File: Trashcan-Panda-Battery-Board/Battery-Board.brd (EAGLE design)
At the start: 77.5 x 45.4 mm, 5 parts, among them J1 B2B-PH-SM4-TB(LF)(SN)

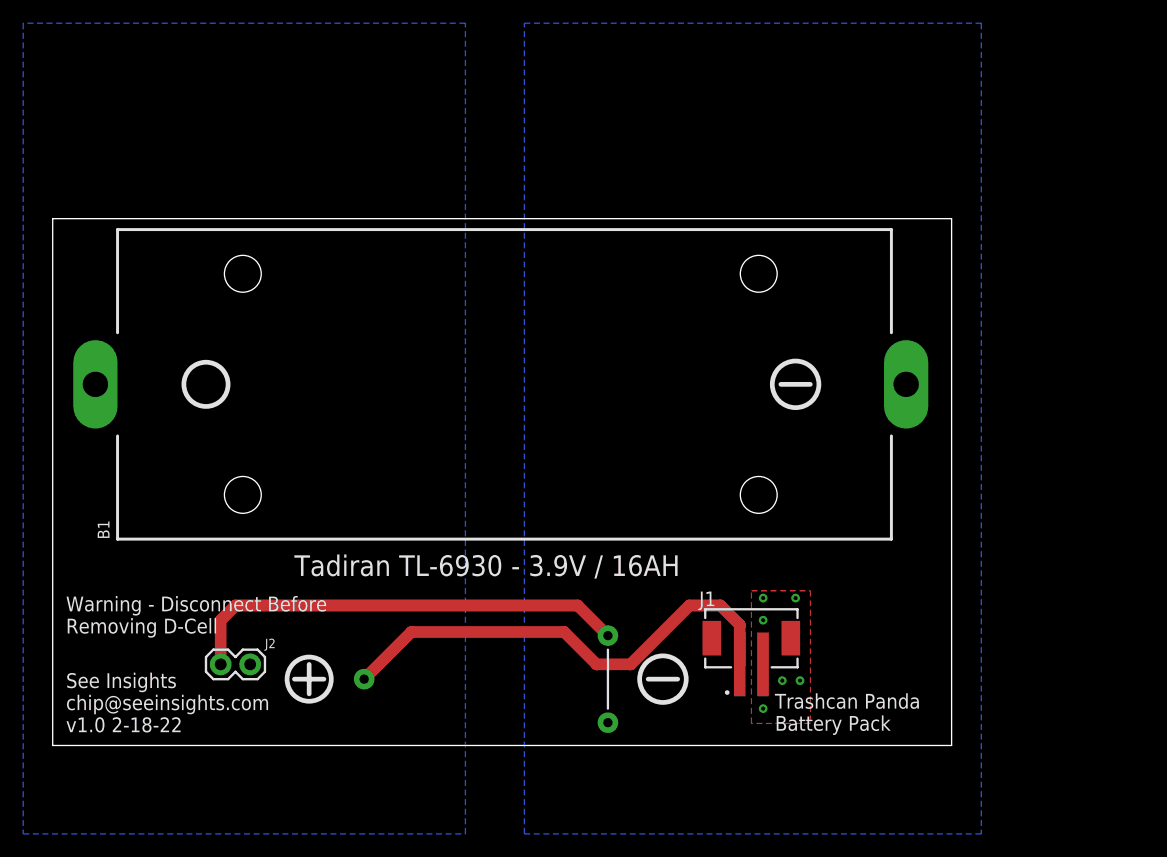
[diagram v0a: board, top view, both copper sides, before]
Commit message: Updated battery board to v1.1
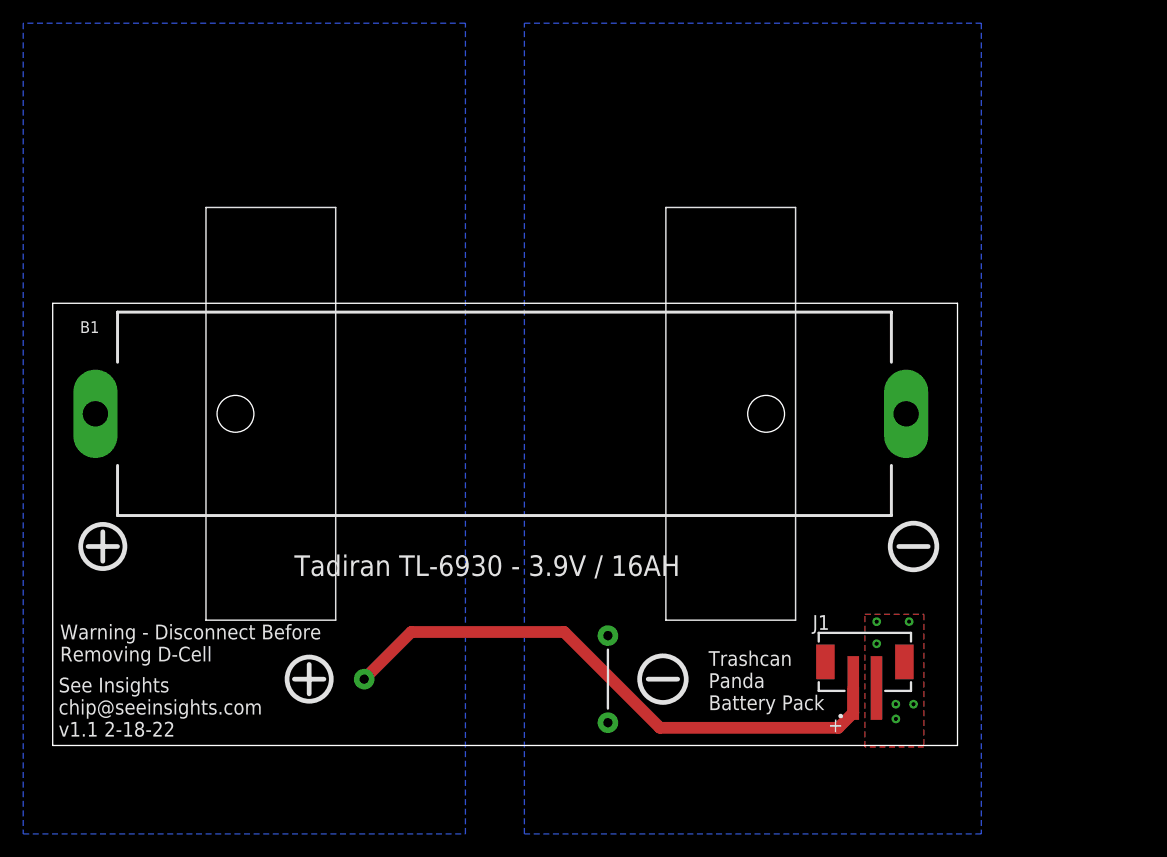
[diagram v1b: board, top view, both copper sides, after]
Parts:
- removed J2: (no value), SparkFun-Connectors:1X02
- B1: value 2226 -> 2232; device Battery-Board:2226 -> Battery-Board:2232
- moved J1 9.99 mm to (70.0, 4.95)
- moved B1 2.54 mm to (38.6, 28.6)
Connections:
- net GND: no longer J2.1
- net VCC: no longer J2.2
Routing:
- net GND: track 38.8 -> 0.00 mm
- net VCC: track 41.4 -> 49.9 mm
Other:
- board size 77.5 x 45.4 mm -> 78 x 38.1 mm
- board text added: "+"
- board text added: "See Insights chip@seeinsights.com v1.1 2-18-22"
- board text removed: "See Insights chip@seeinsights.com v1.0 2-18-22"
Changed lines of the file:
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@@
 <board>
 <plain>
-<wire x1="0" y1="0" x2="77.45" y2="0" width="0" layer="20"/>
-<wire x1="77.45" y1="0" x2="77.45" y2="45.39" width="0" layer="20"/>
-<wire x1="77.45" y1="45.39" x2="0" y2="45.39" width="0" layer="20"/>
-<wire x1="0" y1="45.39" x2="0" y2="0" width="0" layer="20"/>
-<text x="62.23" y="1.27" size="1.27" layer="21">Trashcan Panda
+<wire x1="0" y1="0" x2="77.958" y2="0" width="0" layer="20"/>
+<wire x1="77.958" y1="0" x2="77.958" y2="38.1" width="0" layer="20"/>
+<wire x1="77.958" y1="38.1" x2="0" y2="38.1" width="0" layer="20"/>
+<wire x1="0" y1="38.1" x2="0" y2="0" width="0" layer="20"/>
+<text x="56.515" y="3.048" size="1.27" layer="21">Trashcan
+Panda
 Battery Pack</text>
-<text x="1.143" y="9.652" size="1.27" layer="21">Warning - Disconnect Before
+<text x="0.635" y="7.239" size="1.27" layer="21">Warning - Disconnect Before
 Removing D-Cell</text>
-<text x="1.143" y="1.143" size="1.27" layer="21">See Insights
+<text x="0.508" y="0.762" size="1.27" layer="21">See Insights
 chip@seeinsights.com
-v1.0 2-18-22</text>
+v1.1 2-18-22</text>
 <text x="20.828" y="14.605" size="1.778" layer="21">Tadiran TL-6930 - 3.9V / 16AH</text>
+<text x="66.802" y="1.143" size="1.27" layer="21">+</text>
 </plain>
 <attributes>
@@
 </autorouter>
 <elements>
-<element name="B1" library="Battery-Board" package="2226" override_package3d_urn="urn:adsk.eagle:package:34202687/3" override_package_urn="urn:adsk.eagle:footprint:34202688/1" override_locally_modified="yes" value="2226" x="38.608" y="31.115" smashed="yes">
-<attribute name="AVAILABILITY" value="In Stock" x="38.608" y="31.115" size="1.778" layer="27" display="off"/>
-<attribute name="DESCRIPTION" value="D-Cell Battery Holder" x="38.608" y="31.115" size="1.778" layer="27" display="off"/>
-<attribute name="MF" value="Keystone" x="38.608" y="31.115" size="1.778" layer="27" display="off"/>
-<attribute name="MP" value="2226" x="38.608" y="31.115" size="1.778" layer="27" display="off"/>
-<attribute name="NAME" x="4.8971" y="17.7579" size="1.017690625" layer="25" ratio="18" rot="R90"/>
-<attribute name="PACKAGE" value=" Adafruit Industries" x="38.608" y="31.115" size="1.778" layer="27" display="off"/>
-<attribute name="PRICE" value="None" x="38.608" y="31.115" size="1.778" layer="27" display="off"/>
-<attribute name="PURCHASE-URL" value="https://pricing.snapeda.com/search/part/2226/?ref=eda" x="38.608" y="31.115" size="1.778" layer="27" display="off"/>
-<attribute name="VALUE" x="36.06576875" y="19.0394" size="0.8135125" layer="27" ratio="10"/>
+<element name="B1" library="Battery-Board" package="2232" override_package3d_urn="urn:adsk.eagle:package:34202687/3" override_package_urn="urn:adsk.eagle:footprint:34202688/1" override_locally_modified="yes" value="2232" x="38.608" y="28.575" smashed="yes">
+<attribute name="AVAILABILITY" value="In Stock" x="38.608" y="28.575" size="1.778" layer="27" display="off"/>
+<attribute name="DESCRIPTION" value="D-Cell Battery Holder" x="38.608" y="28.575" size="1.778" layer="27" display="off"/>
+<attribute name="MF" value="Keystone" x="38.608" y="28.575" size="1.778" layer="27" display="off"/>
+<attribute name="MP" value="2226" x="38.608" y="28.575" size="1.778" layer="27" display="off"/>
+<attribute name="NAME" x="2.3571" y="35.5379" size="1.017690625" layer="25" ratio="18"/>
+<attribute name="PACKAGE" value=" Adafruit Industries" x="38.608" y="28.575" size="1.778" layer="27" display="off"/>
+<attribute name="PRICE" value="None" x="38.608" y="28.575" size="1.778" layer="27" display="off"/>
+<attribute name="PURCHASE-URL" value="https://pricing.snapeda.com/search/part/2226/?ref=eda" x="38.608" y="28.575" size="1.778" layer="27" display="off"/>
+<attribute name="VALUE" x="37.33576875" y="17.7694" size="0.8135125" layer="27" ratio="10"/>
 </element>
-<element name="J1" library="Custom Components" package="JST_B2B-PH-SM4-TB(LF)(SN)" value="B2B-PH-SM4-TB(LF)(SN)" x="60.198" y="6.985" smashed="yes">
-<attribute name="DESCRIPTION" value=" Connector Header Surface Mount 2 position 0.079 (2.00mm) " x="60.198" y="6.985" size="1.778" layer="27" display="off"/>
-<attribute name="DIGI-KEY_PART_NUMBER" value="455-1734-1-ND" x="60.198" y="6.985" size="1.778" layer="27" display="off"/>
-<attribute name="MF" value="JST Sales" x="60.198" y="6.985" size="1.778" layer="27" display="off"/>
-<attribute name="MP" value="B2B-PH-SM4-TB(LF)(SN)" x="60.198" y="6.985" size="1.778" layer="27" display="off"/>
-<attribute name="NAME" x="55.69218125" y="11.99146875" size="1.271640625" layer="25"/>
-<attribute name="PACKAGE" value="None" x="60.198" y="6.985" size="1.778" layer="27" display="off"/>
-<attribute name="PURCHASE-URL" value="https://pricing.snapeda.com/search/part/B2B-PH-SM4-TB(LF)(SN)/?ref=eda" x="60.198" y="6.985" size="1.778" layer="27" display="off"/>
-</element>
-<element name="J2" library="SparkFun-Connectors" library_urn="urn:adsk.eagle:library:513" package="1X02" package3d_urn="urn:adsk.eagle:package:38039/1" value="" x="14.478" y="6.985" smashed="yes">
-<attribute name="NAME" x="18.288" y="8.382" size="0.8128" layer="25" font="vector"/>
-<attribute name="VALUE" x="13.208" y="4.953" size="0.6096" layer="27" font="vector" ratio="20"/>
+<element name="J1" library="Custom Components" package="JST_B2B-PH-SM4-TB(LF)(SN)" value="B2B-PH-SM4-TB(LF)(SN)" x="69.977" y="4.953" smashed="yes">
+<attribute name="DESCRIPTION" value=" Connector Header Surface Mount 2 position 0.079 (2.00mm) " x="69.977" y="4.953" size="1.778" layer="27" display="off"/>
+<attribute name="DIGI-KEY_PART_NUMBER" value="455-1734-1-ND" x="69.977" y="4.953" size="1.778" layer="27" display="off"/>
+<attribute name="MF" value="JST Sales" x="69.977" y="4.953" size="1.778" layer="27" display="off"/>
+<attribute name="MP" value="B2B-PH-SM4-TB(LF)(SN)" x="69.977" y="4.953" size="1.778" layer="27" display="off"/>
+<attribute name="NAME" x="65.47118125" y="9.95946875" size="1.271640625" layer="25"/>
+<attribute name="PACKAGE" value="None" x="69.977" y="4.953" size="1.778" layer="27" display="off"/>
+<attribute name="PURCHASE-URL" value="https://pricing.snapeda.com/search/part/B2B-PH-SM4-TB(LF)(SN)/?ref=eda" x="69.977" y="4.953" size="1.778" layer="27" display="off"/>
 </element>
 <element name="U$1" library="Battery-Board" package="HLC-1520A/TP" value="HLC-1520A/TP" x="37.338" y="5.715" smashed="yes">
@@
 <vertex x="35.56" y="-7.62"/>
 </polygon>
-<contactref element="J2" pad="2"/>
 <contactref element="J1" pad="1"/>
 <contactref element="U$1" pad="+"/>
@@
 <wire x1="26.838" y1="5.715" x2="30.902" y2="9.779" width="1.016" layer="1"/>
 <wire x1="30.902" y1="9.779" x2="44.069" y2="9.779" width="1.016" layer="1"/>
-<wire x1="44.069" y1="9.779" x2="46.863" y2="6.985" width="1.016" layer="1"/>
-<wire x1="49.784" y1="6.985" x2="54.864" y2="12.065" width="1.016" layer="1"/>
-<wire x1="54.864" y1="12.065" x2="57.531" y2="12.065" width="1.016" layer="1"/>
-<wire x1="59.198" y1="10.398" x2="59.198" y2="6.985" width="1.016" layer="1"/>
-<wire x1="46.863" y1="6.985" x2="49.784" y2="6.985" width="1.016" layer="1"/>
-<wire x1="57.531" y1="12.065" x2="59.198" y2="10.398" width="1.016" layer="1"/>
+<wire x1="52.324" y1="1.524" x2="67.691" y2="1.524" width="1.016" layer="1"/>
+<wire x1="67.691" y1="1.524" x2="68.977" y2="2.81" width="1.016" layer="1"/>
+<wire x1="68.977" y1="2.81" x2="68.977" y2="4.953" width="1.016" layer="1"/>
+<wire x1="44.069" y1="9.779" x2="52.324" y2="1.524" width="1.016" layer="1"/>
+<wire x1="26.838" y1="5.715" x2="3.683" y2="28.575" width="0" layer="19" extent="1-1"/>
 </signal>
 <signal name="GND">
@@
 <vertex x="40.64" y="-7.62"/>
 </polygon>
-<contactref element="J2" pad="1"/>
 <contactref element="J1" pad="2"/>
 <contactref element="U$1" pad="--"/>
 <contactref element="U$1" pad="-"/>
 <contactref element="B1" pad="-"/>
-<wire x1="47.838" y1="9.465" x2="45.238" y2="12.065" width="1.016" layer="1"/>
-<wire x1="45.238" y1="12.065" x2="15.748" y2="12.065" width="1.016" layer="1"/>
-<wire x1="15.748" y1="12.065" x2="14.478" y2="10.795" width="1.016" layer="1"/>
-<wire x1="14.478" y1="10.795" x2="14.478" y2="6.985" width="1.016" layer="1"/>
 <polygon width="0.1524" layer="1">
-<vertex x="60.198" y="13.335"/>
-<vertex x="65.278" y="13.335"/>
-<vertex x="65.278" y="1.905"/>
-<vertex x="60.198" y="1.905"/>
+<vertex x="69.977" y="11.303"/>
+<vertex x="75.057" y="11.303"/>
+<vertex x="75.057" y="-0.127"/>
+<vertex x="69.977" y="-0.127"/>
 </polygon>
-<via x="61.214" y="10.795" extent="1-16" drill="0.35"/>
-<via x="62.865" y="5.588" extent="1-16" drill="0.35"/>
-<via x="64.389" y="5.588" extent="1-16" drill="0.35"/>
-<via x="61.214" y="3.175" extent="1-16" drill="0.35"/>
-<via x="64.008" y="12.7" extent="1-16" drill="0.35"/>
-<via x="61.214" y="12.7" extent="1-16" drill="0.35"/>
+<via x="70.993" y="8.763" extent="1-16" drill="0.35"/>
+<via x="72.644" y="3.556" extent="1-16" drill="0.35"/>
+<via x="74.168" y="3.556" extent="1-16" drill="0.35"/>
+<via x="72.644" y="2.286" extent="1-16" drill="0.35"/>
+<via x="73.787" y="10.668" extent="1-16" drill="0.35"/>
+<via x="70.993" y="10.668" extent="1-16" drill="0.35"/>
+<wire x1="73.787" y1="10.668" x2="73.533" y2="28.575" width="0" layer="19" extent="1-1"/>
+<wire x1="70.993" y1="10.668" x2="73.787" y2="10.668" width="0" layer="19" extent="1-1"/>
+<wire x1="70.993" y1="8.763" x2="70.993" y2="10.668" width="0" layer="19" extent="1-1"/>
+<wire x1="70.977" y1="4.953" x2="70.993" y2="8.763" width="0" layer="19" extent="1-1"/>
+<wire x1="72.644" y1="3.556" x2="70.977" y2="4.953" width="0" layer="19" extent="1-1"/>
+<wire x1="74.168" y1="3.556" x2="72.644" y2="3.556" width="0" layer="19" extent="1-1"/>
+<wire x1="72.644" y1="2.286" x2="72.644" y2="3.556" width="0" layer="19" extent="1-1"/>
+<wire x1="47.838" y1="1.965" x2="72.644" y2="2.286" width="0" layer="19" extent="1-1"/>
+<wire x1="47.838" y1="9.465" x2="47.838" y2="1.965" width="0" layer="19" extent="1-1"/>
 </signal>
 </signals>

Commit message: Changed Battery Board Profile
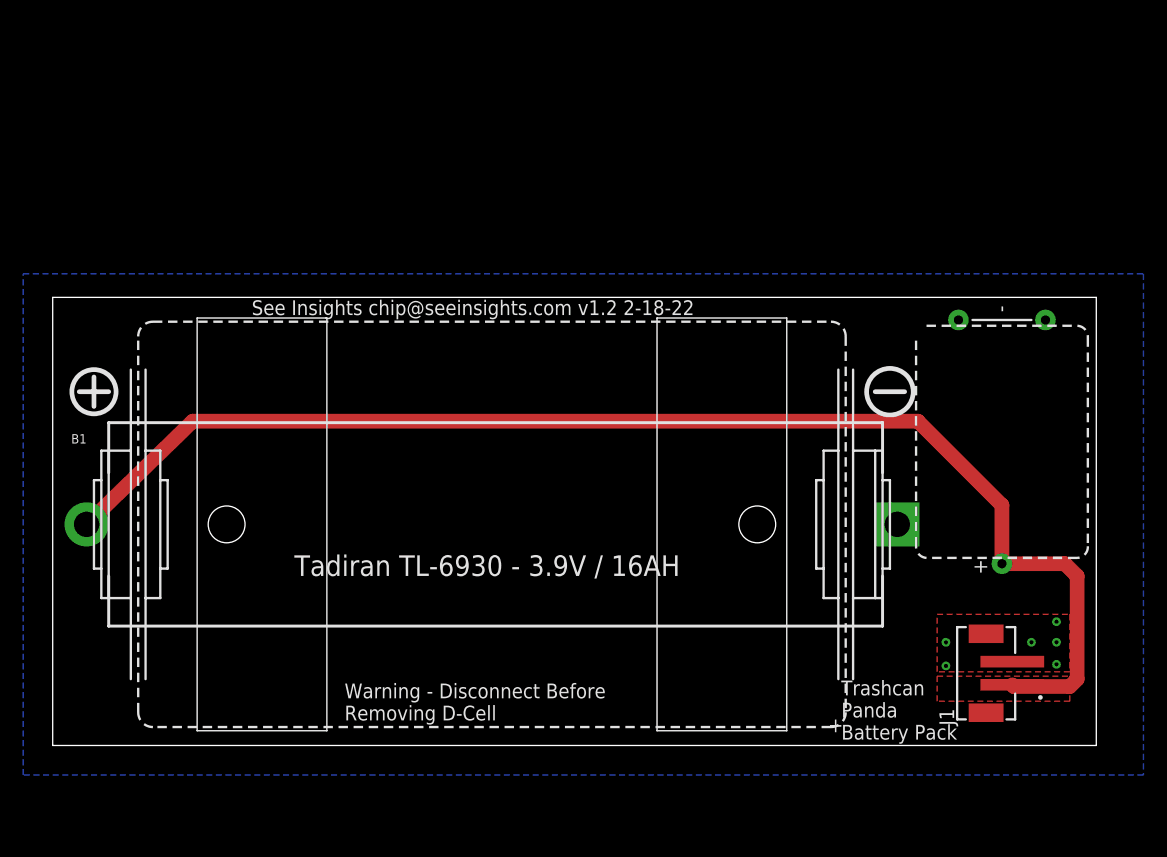
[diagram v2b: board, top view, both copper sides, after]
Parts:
- moved U$1 48.9 mm to (81.8, 26.2), turned to 90 degrees
- moved J1 12.8 mm to (82.7, 6.22), turned to 90 degrees
- moved B1 9.56 mm to (37.8, 19.1)
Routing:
- net VCC: track 49.9 -> 112.2 mm
- added copper zone on layer 1, net VCC
- removed copper zone on layer 16, net VCC
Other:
- board size 78 x 38.1 mm -> 89.9 x 38.6 mm
- board text added: "See Insights chip@seeinsights.com v1.2 2-18-22"
- board text removed: "See Insights chip@seeinsights.com v1.1 2-18-22"
